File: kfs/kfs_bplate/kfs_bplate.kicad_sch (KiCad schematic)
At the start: 10 parts

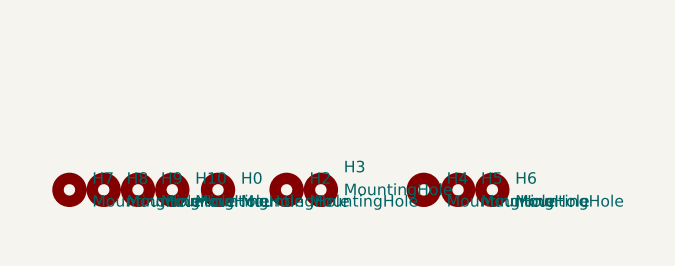
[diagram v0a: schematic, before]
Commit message: Slight mods to kfs.
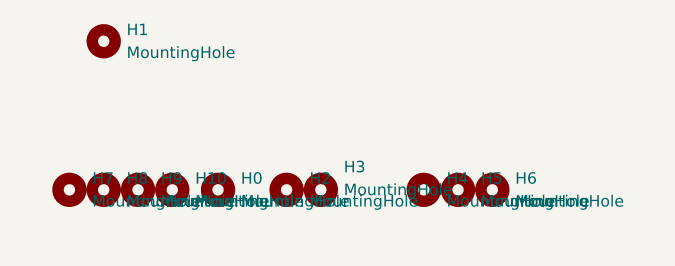
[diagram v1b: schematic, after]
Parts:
- added H1: MountingHole, MountingHole:MountingHole_4mm, symbol Mechanical:MountingHole
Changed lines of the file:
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@@
+    )
+  )
+  (symbol (lib_id "Mechanical:MountingHole") (at 257.81 137.16 0) (unit 1)
+    (in_bom yes) (on_board yes) (dnp no) (fields_autoplaced)
+    (property "Reference" "H1" (at 260.35 135.89 0)
+      (effects (font (size 1.27 1.27)) (justify left))
+    )
+    (property "Value" "MountingHole" (at 260.35 138.43 0)
+      (effects (font (size 1.27 1.27)) (justify left))
+    )
+    (property "Footprint" "MountingHole:MountingHole_4mm" (at 257.81 137.16 0)
+      (effects (font (size 1.27 1.27)) hide)
+    )
+    (property "Datasheet" "~" (at 257.81 137.16 0)
+      (effects (font (size 1.27 1.27)) hide)
+    )
+    (instances
+      (project "kfs_bplate"
+        (path "/97127b28-60f4-45ff-835e-dccfbc833331"
+          (reference "H1") (unit 1)
+        )
+      )
     )
   )

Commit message: Switched to staggered kfs layout.
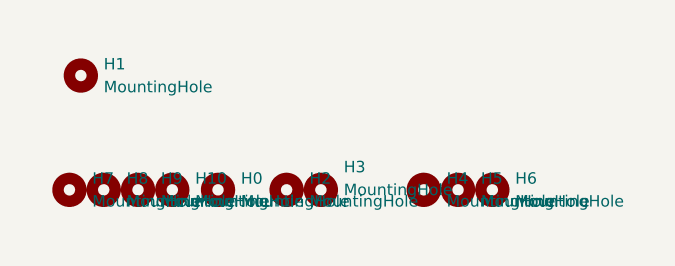
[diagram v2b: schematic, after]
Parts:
- H1: footprint MountingHole:MountingHole_4mm -> MountingHole:MountingHole_8.4mm_M8
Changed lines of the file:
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@@
-    )
-  )
-  (symbol (lib_id "Mechanical:MountingHole") (at 257.81 137.16 0) (unit 1)
-    (in_bom yes) (on_board yes) (dnp no) (fields_autoplaced)
-    (property "Reference" "H1" (at 260.35 135.89 0)
-      (effects (font (size 1.27 1.27)) (justify left))
-    )
-    (property "Value" "MountingHole" (at 260.35 138.43 0)
-      (effects (font (size 1.27 1.27)) (justify left))
-    )
-    (property "Footprint" "MountingHole:MountingHole_4mm" (at 257.81 137.16 0)
-      (effects (font (size 1.27 1.27)) hide)
-    )
-    (property "Datasheet" "~" (at 257.81 137.16 0)
-      (effects (font (size 1.27 1.27)) hide)
-    )
-    (instances
-      (project "kfs_bplate"
-        (path "/97127b28-60f4-45ff-835e-dccfbc833331"
-          (reference "H1") (unit 1)
-        )
-      )
     )
   )
@@
         )
       )
+    )
+  )
+  (symbol (lib_id "Mechanical:MountingHole") (at 255.27 140.97 0) (unit 1)
+    (in_bom yes) (on_board yes) (dnp no) (fields_autoplaced)
+    (property "Reference" "H1" (at 257.81 139.7 0)
+      (effects (font (size 1.27 1.27)) (justify left))
+    )
+    (property "Value" "MountingHole" (at 257.81 142.24 0)
+      (effects (font (size 1.27 1.27)) (justify left))
+    )
+    (property "Footprint" "MountingHole:MountingHole_8.4mm_M8" (at 255.27 140.97 0)
+      (effects (font (size 1.27 1.27)) hide)
+    )
+    (property "Datasheet" "~" (at 255.27 140.97 0)
+      (effects (font (size 1.27 1.27)) hide)
+    )
+    (instances
+      (project "kfs_bplate"
+        (path "/97127b28-60f4-45ff-835e-dccfbc833331"
+          (reference "H1") (unit 1)
+        )
+      )

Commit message: Moved the bottom row of kfs farther inward.
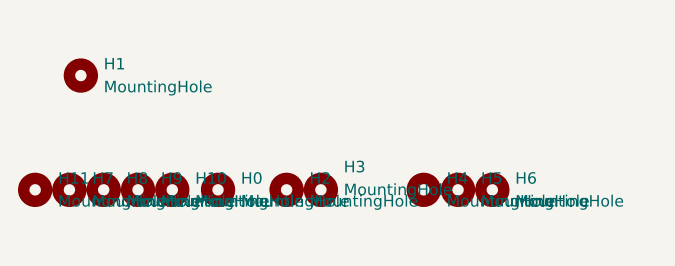
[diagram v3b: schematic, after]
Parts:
- added H11: MountingHole, MountingHole:MountingHole_2.2mm_M2_ISO7380_Pad, symbol Mechanical:MountingHole
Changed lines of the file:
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@@
+    )
+  )
+  (symbol (lib_id "Mechanical:MountingHole") (at 250.19 153.67 0) (unit 1)
+    (in_bom yes) (on_board yes) (dnp no) (fields_autoplaced)
+    (property "Reference" "H11" (at 252.73 152.4 0)
+      (effects (font (size 1.27 1.27)) (justify left))
+    )
+    (property "Value" "MountingHole" (at 252.73 154.94 0)
+      (effects (font (size 1.27 1.27)) (justify left))
+    )
+    (property "Footprint" "MountingHole:MountingHole_2.2mm_M2_ISO7380_Pad" (at 250.19 153.67 0)
+      (effects (font (size 1.27 1.27)) hide)
+    )
+    (property "Datasheet" "~" (at 250.19 153.67 0)
+      (effects (font (size 1.27 1.27)) hide)
+    )
+    (instances
+      (project "kfs_bplate"
+        (path "/97127b28-60f4-45ff-835e-dccfbc833331"
+          (reference "H11") (unit 1)
+        )
+      )
     )
   )

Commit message: Updated reset button and mounting holes on kfs.
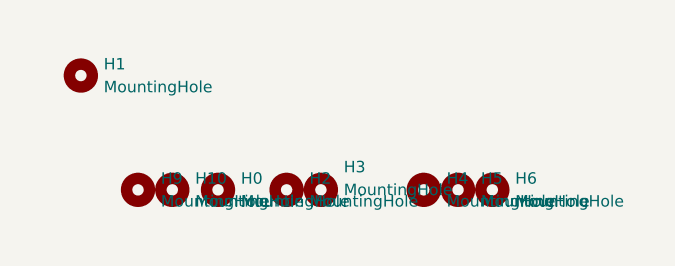
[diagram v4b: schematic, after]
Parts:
- removed H11, H7, H8: MountingHole, MountingHole:MountingHole_2.2mm_M2_ISO7380_Pad, symbol Mechanical:MountingHole
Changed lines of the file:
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@@
-    )
-  )
-  (symbol (lib_id "Mechanical:MountingHole") (at 254 153.67 0) (unit 1)
-    (in_bom yes) (on_board yes) (dnp no) (fields_autoplaced)
-    (property "Reference" "H7" (at 256.54 152.4 0)
-      (effects (font (size 1.27 1.27)) (justify left))
-    )
-    (property "Value" "MountingHole" (at 256.54 154.94 0)
-      (effects (font (size 1.27 1.27)) (justify left))
-    )
-    (property "Footprint" "MountingHole:MountingHole_2.2mm_M2_ISO7380_Pad" (at 254 153.67 0)
-      (effects (font (size 1.27 1.27)) hide)
-    )
-    (property "Datasheet" "~" (at 254 153.67 0)
-      (effects (font (size 1.27 1.27)) hide)
-    )
-    (instances
-      (project "kfs_bplate"
-        (path "/97127b28-60f4-45ff-835e-dccfbc833331"
-          (reference "H7") (unit 1)
-        )
-      )
     )
   )
@@
         )
       )
-    )
-  )
-  (symbol (lib_id "Mechanical:MountingHole") (at 257.81 153.67 0) (unit 1)
-    (in_bom yes) (on_board yes) (dnp no) (fields_autoplaced)
-    (property "Reference" "H8" (at 260.35 152.4 0)
-      (effects (font (size 1.27 1.27)) (justify left))
-    )
-    (property "Value" "MountingHole" (at 260.35 154.94 0)
-      (effects (font (size 1.27 1.27)) (justify left))
-    )
-    (property "Footprint" "MountingHole:MountingHole_2.2mm_M2_ISO7380_Pad" (at 257.81 153.67 0)
-      (effects (font (size 1.27 1.27)) hide)
-    )
-    (property "Datasheet" "~" (at 257.81 153.67 0)
-      (effects (font (size 1.27 1.27)) hide)
-    )
-    (instances
-      (project "kfs_bplate"
-        (path "/97127b28-60f4-45ff-835e-dccfbc833331"
-          (reference "H8") (unit 1)
-        )
-      )
-    )
-  )
-  (symbol (lib_id "Mechanical:MountingHole") (at 250.19 153.67 0) (unit 1)
-    (in_bom yes) (on_board yes) (dnp no) (fields_autoplaced)
-    (property "Reference" "H11" (at 252.73 152.4 0)
-      (effects (font (size 1.27 1.27)) (justify left))
-    )
-    (property "Value" "MountingHole" (at 252.73 154.94 0)
-      (effects (font (size 1.27 1.27)) (justify left))
-    )
-    (property "Footprint" "MountingHole:MountingHole_2.2mm_M2_ISO7380_Pad" (at 250.19 153.67 0)
-      (effects (font (size 1.27 1.27)) hide)
-    )
-    (property "Datasheet" "~" (at 250.19 153.67 0)
-      (effects (font (size 1.27 1.27)) hide)
-    )
-    (instances
-      (project "kfs_bplate"
-        (path "/97127b28-60f4-45ff-835e-dccfbc833331"
-          (reference "H11") (unit 1)
-        )
-      )

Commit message: Changed reset button again. Removed some standoffs.
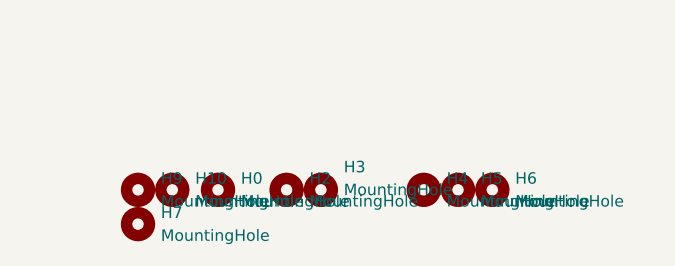
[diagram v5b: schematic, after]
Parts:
- removed H1: MountingHole, MountingHole:MountingHole_8.4mm_M8, symbol Mechanical:MountingHole
- added H7: MountingHole, MountingHole:MountingHole_2.2mm_M2_ISO7380_Pad, symbol Mechanical:MountingHole
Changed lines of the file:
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@@
-    )
-  )
-  (symbol (lib_id "Mechanical:MountingHole") (at 255.27 140.97 0) (unit 1)
-    (in_bom yes) (on_board yes) (dnp no) (fields_autoplaced)
-    (property "Reference" "H1" (at 257.81 139.7 0)
-      (effects (font (size 1.27 1.27)) (justify left))
-    )
-    (property "Value" "MountingHole" (at 257.81 142.24 0)
-      (effects (font (size 1.27 1.27)) (justify left))
-    )
-    (property "Footprint" "MountingHole:MountingHole_8.4mm_M8" (at 255.27 140.97 0)
-      (effects (font (size 1.27 1.27)) hide)
-    )
-    (property "Datasheet" "~" (at 255.27 140.97 0)
-      (effects (font (size 1.27 1.27)) hide)
-    )
-    (instances
-      (project "kfs_bplate"
-        (path "/97127b28-60f4-45ff-835e-dccfbc833331"
-          (reference "H1") (unit 1)
-        )
-      )
     )
   )
@@
         )
       )
+    )
+  )
+  (symbol (lib_id "Mechanical:MountingHole") (at 261.62 157.48 0) (unit 1)
+    (in_bom yes) (on_board yes) (dnp no) (fields_autoplaced)
+    (property "Reference" "H7" (at 264.16 156.21 0)
+      (effects (font (size 1.27 1.27)) (justify left))
+    )
+    (property "Value" "MountingHole" (at 264.16 158.75 0)
+      (effects (font (size 1.27 1.27)) (justify left))
+    )
+    (property "Footprint" "MountingHole:MountingHole_2.2mm_M2_ISO7380_Pad" (at 261.62 157.48 0)
+      (effects (font (size 1.27 1.27)) hide)
+    )
+    (property "Datasheet" "~" (at 261.62 157.48 0)
+      (effects (font (size 1.27 1.27)) hide)
+    )
+    (instances
+      (project "kfs_bplate"
+        (path "/97127b28-60f4-45ff-835e-dccfbc833331"
+          (reference "H7") (unit 1)
+        )
+      )

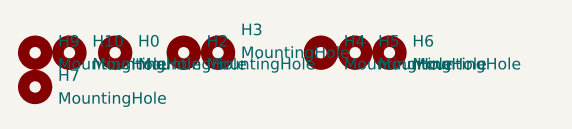
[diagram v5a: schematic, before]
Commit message: Switched kfs to use nice!nano.
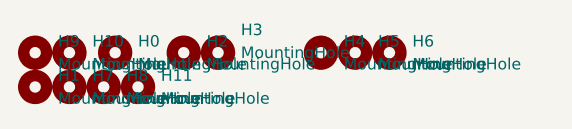
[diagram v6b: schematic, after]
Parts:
- added H1, H11, H8: MountingHole, MountingHole:MountingHole_2.2mm_M2_ISO7380_Pad, symbol Mechanical:MountingHole
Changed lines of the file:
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@@
+    )
+  )
+  (symbol (lib_id "Mechanical:MountingHole") (at 261.62 157.48 0) (unit 1)
+    (in_bom yes) (on_board yes) (dnp no) (fields_autoplaced)
+    (property "Reference" "H1" (at 264.16 156.21 0)
+      (effects (font (size 1.27 1.27)) (justify left))
+    )
+    (property "Value" "MountingHole" (at 264.16 158.75 0)
+      (effects (font (size 1.27 1.27)) (justify left))
+    )
+    (property "Footprint" "MountingHole:MountingHole_2.2mm_M2_ISO7380_Pad" (at 261.62 157.48 0)
+      (effects (font (size 1.27 1.27)) hide)
+    )
+    (property "Datasheet" "~" (at 261.62 157.48 0)
+      (effects (font (size 1.27 1.27)) hide)
+    )
+    (instances
+      (project "kfs_bplate"
+        (path "/97127b28-60f4-45ff-835e-dccfbc833331"
+          (reference "H1") (unit 1)
+        )
+      )
     )
   )
@@
         (path "/97127b28-60f4-45ff-835e-dccfbc833331"
           (reference "H3") (unit 1)
+        )
+      )
+    )
+  )
+  (symbol (lib_id "Mechanical:MountingHole") (at 265.43 157.48 0) (unit 1)
+    (in_bom yes) (on_board yes) (dnp no) (fields_autoplaced)
+    (property "Reference" "H7" (at 267.97 156.21 0)
+      (effects (font (size 1.27 1.27)) (justify left))
+    )
+    (property "Value" "MountingHole" (at 267.97 158.75 0)
+      (effects (font (size 1.27 1.27)) (justify left))
+    )
+    (property "Footprint" "MountingHole:MountingHole_2.2mm_M2_ISO7380_Pad" (at 265.43 157.48 0)
+      (effects (font (size 1.27 1.27)) hide)
+    )
+    (property "Datasheet" "~" (at 265.43 157.48 0)
+      (effects (font (size 1.27 1.27)) hide)
+    )
+    (instances
+      (project "kfs_bplate"
+        (path "/97127b28-60f4-45ff-835e-dccfbc833331"
+          (reference "H7") (unit 1)
         )
       )
@@
     )
   )
+  (symbol (lib_id "Mechanical:MountingHole") (at 269.24 157.48 0) (unit 1)
+    (in_bom yes) (on_board yes) (dnp no) (fields_autoplaced)
+    (property "Reference" "H8" (at 271.78 156.21 0)
+      (effects (font (size 1.27 1.27)) (justify left))
+    )
+    (property "Value" "MountingHole" (at 271.78 158.75 0)
+      (effects (font (size 1.27 1.27)) (justify left))
+    )
+    (property "Footprint" "MountingHole:MountingHole_2.2mm_M2_ISO7380_Pad" (at 269.24 157.48 0)
+      (effects (font (size 1.27 1.27)) hide)
+    )
+    (property "Datasheet" "~" (at 269.24 157.48 0)
+      (effects (font (size 1.27 1.27)) hide)
+    )
+    (instances
+      (project "kfs_bplate"
+        (path "/97127b28-60f4-45ff-835e-dccfbc833331"
+          (reference "H8") (unit 1)
+        )
+      )
+    )
+  )
   (symbol (lib_id "Mechanical:MountingHole") (at 261.62 153.67 0) (unit 1)
     (in_bom yes) (on_board yes) (dnp no) (fields_autoplaced)
@@
     )
   )
-  (symbol (lib_id "Mechanical:MountingHole") (at 261.62 157.48 0) (unit 1)
+  (symbol (lib_id "Mechanical:MountingHole") (at 273.05 157.48 0) (unit 1)
     (in_bom yes) (on_board yes) (dnp no) (fields_autoplaced)
-    (property "Reference" "H7" (at 264.16 156.21 0)
+    (property "Reference" "H11" (at 275.59 156.21 0)
       (effects (font (size 1.27 1.27)) (justify left))
     )
-    (property "Value" "MountingHole" (at 264.16 158.75 0)
+    (property "Value" "MountingHole" (at 275.59 158.75 0)
       (effects (font (size 1.27 1.27)) (justify left))
     )
-    (property "Footprint" "MountingHole:MountingHole_2.2mm_M2_ISO7380_Pad" (at 261.62 157.48 0)
+    (property "Footprint" "MountingHole:MountingHole_2.2mm_M2_ISO7380_Pad" (at 273.05 157.48 0)
       (effects (font (size 1.27 1.27)) hide)
     )
-    (property "Datasheet" "~" (at 261.62 157.48 0)
+    (property "Datasheet" "~" (at 273.05 157.48 0)
       (effects (font (size 1.27 1.27)) hide)
     )
@@
       (project "kfs_bplate"
         (path "/97127b28-60f4-45ff-835e-dccfbc833331"
-          (reference "H7") (unit 1)
+          (reference "H11") (unit 1)
         )
       )
